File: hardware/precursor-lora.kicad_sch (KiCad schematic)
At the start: 3 parts, among them U2 AP2112K-3.3

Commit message: Fix schematic: add all components and connections
Previous schematic was incomplete skeleton. Now includes:
- U1: RAK3172 module with all 32 pins
- U2: AP2112K-3.3 LDO regulator
- C1, C2: 10uF input/output capacitors
- C3, C4: 100nF decoupling capacitors
- R1: 10K reset pullup
- R2: 10K BOOT0 pulldown
- R3: 1K LED current limit
- LED1: Power indicator
- J1: 8-pin Precursor connector
- J2: U.FL RF connector
- All power symbols and wire connections
- Annotation text for clarity

Embedded lib_symbols so file opens standalone in KiCad 8.
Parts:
- added C3, C4: 100nF, Capacitor_SMD:C_0402_1005Metric, symbol Device:C
- added J1: PRECURSOR_CONN, Connector_PinHeader_1.27mm:PinHeader_2x04_P1.27mm_Vertical, symbol Connector:Conn_01x08_Pin
- added J2: U.FL, Connector_Coaxial:U.FL_Hirose_U.FL-R-SMT-1_Vertical, symbol Connector:Conn_Coaxial
- added LED1: GREEN, LED_SMD:LED_0603_1608Metric, symbol Device:LED
- added R1, R2: 10K, Resistor_SMD:R_0402_1005Metric, symbol Device:R
- added R3: 1K, Resistor_SMD:R_0402_1005Metric, symbol Device:R
- added U1: RAK3172, PrecursorLoRa:RAK3172, symbol PrecursorLoRa:RAK3172
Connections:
- net GND: now also C1.2, C2.2, U2.2 (GND), C3.2, C4.2, J2.2 (Ext), LED1.1 (K), R2.2, U1.23 (GND), U1.28 (GND)
- net VIN_3V7: now also C1.1, U2.1 (VIN), U2.3 (EN)
- new net: J2.1 (In), U1.12 (RF)
- new net: R2.1, U1.22 (BOOT0)
- new net: J1.6 (Pin_6), U1.3 (PA15)
- new net: J1.7 (Pin_7), U1.4 (PB6/UART1_TX)
- new net: R1.2, U1.6 (PA1)
- new net: LED1.2 (A), R3.2
- new net +3V3: C2.1, C3.1, C4.1, R1.1, R3.1, U1.24 (VDD), U2.5 (VOUT)
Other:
- note added: "BOOT0 PULLDOWN (Normal operation)"
- note added: "DECOUPLING CAPACITORS"
- note added: "POWER LED"
- note added: "POWER SUPPLY 3.7V LiPo -> 3.3V LDO"
- note added: "PRECURSOR LORA EXPANSION MODULE Power: 3.7V LiPo -> AP2112K LDO -> 3.3V Interface: UART1 (PB6/PB7) to Precursor FPGA RF: U.FL connector to external antenna"
- note added: "Pin Assignments: 1: UART_TX (to Precursor RX) 2: UART_RX (from Precursor TX) 3: ~RST (active low reset) 4: BUSY (status output) 5: VIN (3.7V) 6: GND 7: NC 8: NC"
- note added: "RESET PULLUP"
- note added: "To Precursor GPIO Header"
- note added: "U.FL RF Connector"
- note removed: "Connector to Precursor 8-pin 1.27mm pitch header"
- note removed: "Power Supply Section Input: 3.7V LiPo Output: 3.3V via AP2112K LDO"
- note removed: "RAK3172 LoRa Module UART1: PB6(TX), PB7(RX) - Primary interface UART2: PA2(TX), PA3(RX) - AT commands"

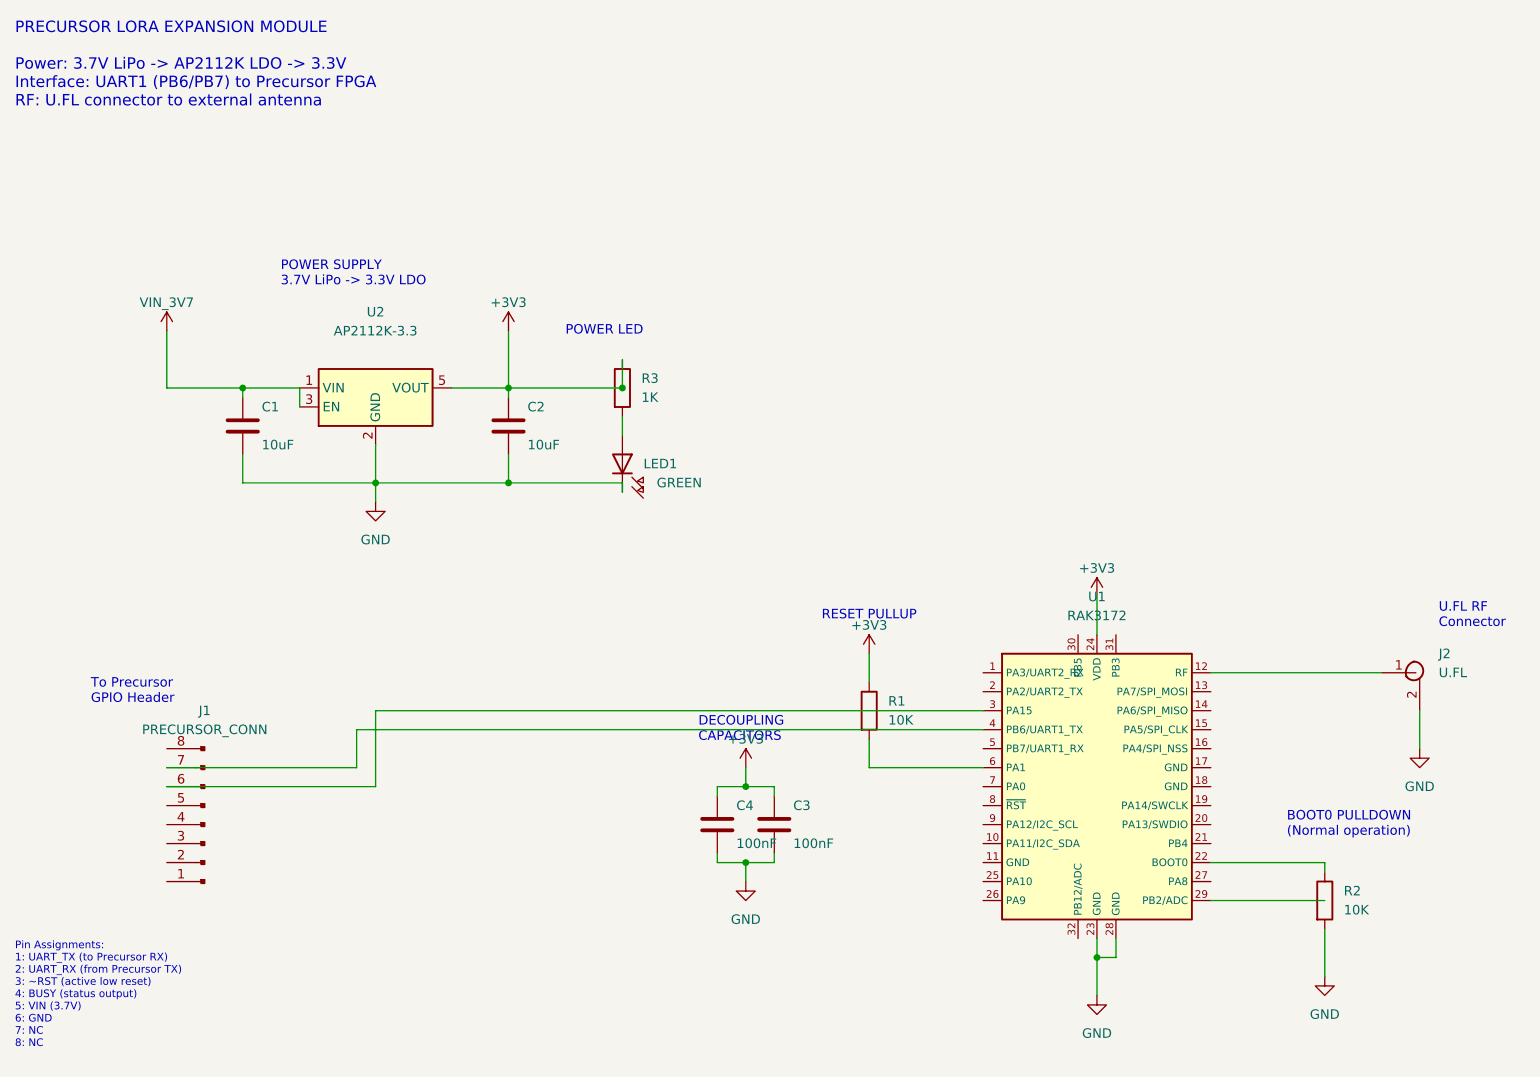
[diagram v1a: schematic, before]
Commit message: Fix schematic wire connections
Corrected wire routing:
- J1.1 now connects to RAK3172 PB6/UART1_TX (pin 4)
- J1.2 now connects to RAK3172 PB7/UART1_RX (pin 5)
- RF wire now correctly routes from RAK3172 pin 12 to U.FL
- Added J1.4 (BUSY) connection to RAK3172 PB5 (pin 30)
- Added J1.5 (VIN) connection to power rail
- Added J1.6 (GND) with GND symbol
- LDO EN pin connected to VIN for always-on operation
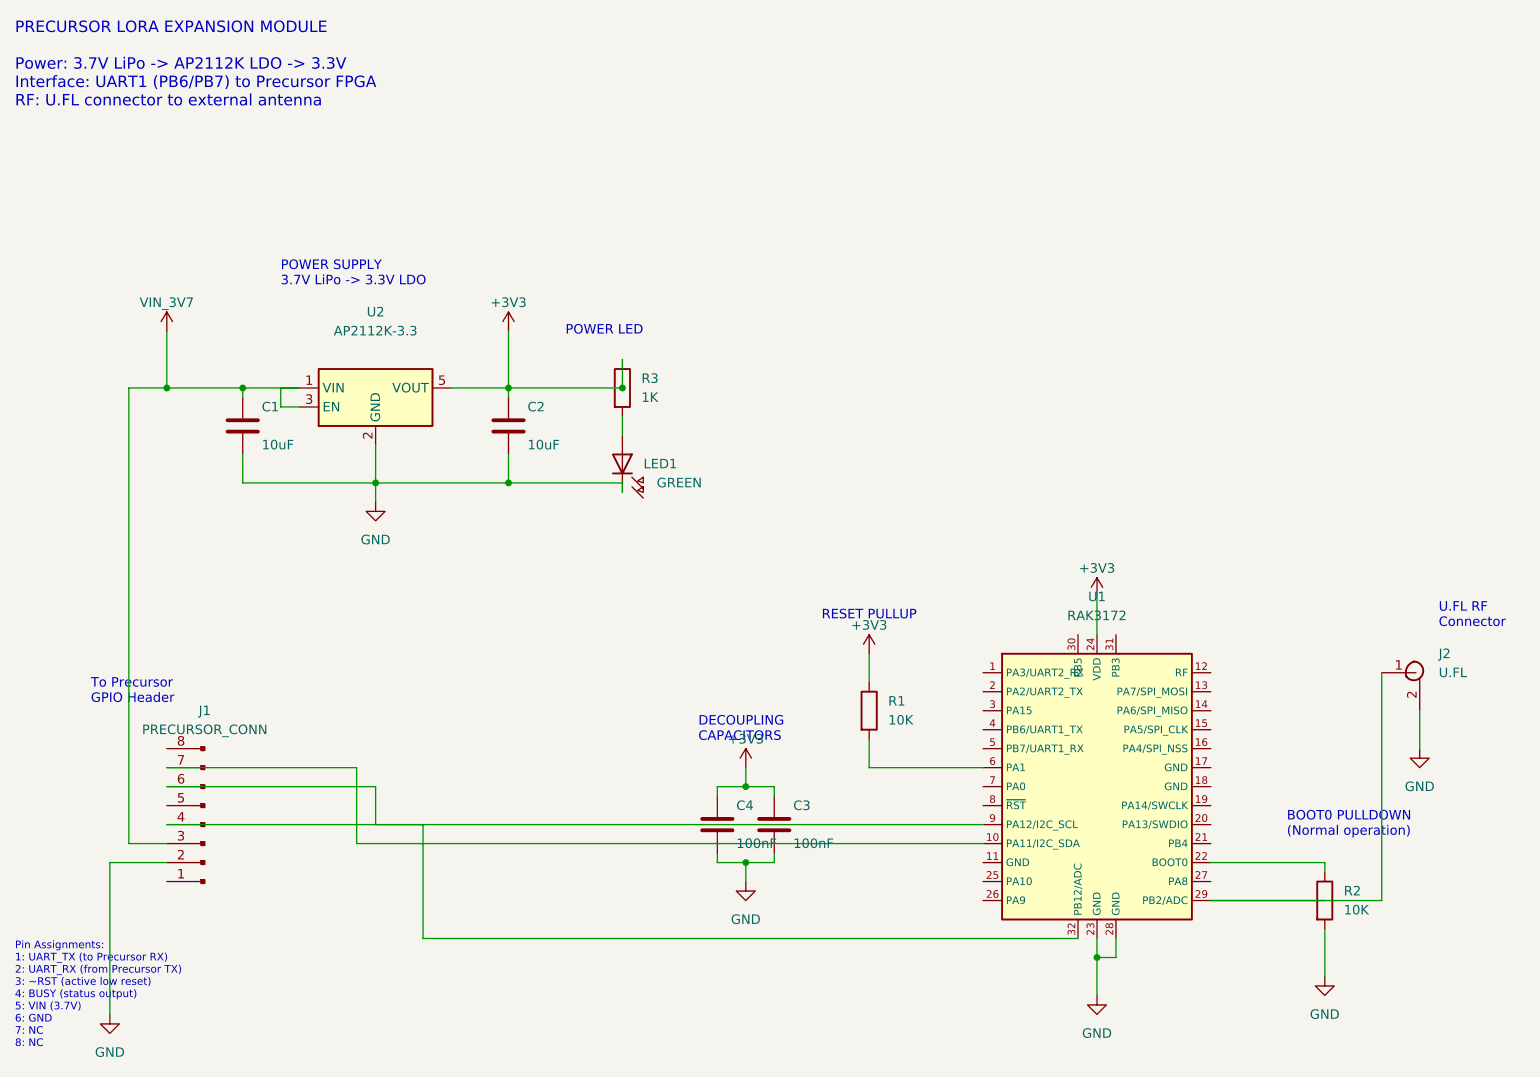
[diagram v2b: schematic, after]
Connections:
- net GND: now also J1.2 (Pin_2)
- net VIN_3V7: now also J1.3 (Pin_3)
- net at U1.10 (PA11/I2C_SDA): now also J1.7 (Pin_7)
- net at U1.12 (RF): no longer J2.1 (In)
- net at U1.29 (PB2/ADC): now also J2.1 (In)
- net at U1.3 (PA15): no longer J1.6 (Pin_6)
- net at U1.32 (PB12/ADC): now also J1.4 (Pin_4), J1.6 (Pin_6), U1.9 (PA12/I2C_SCL)
- net at U1.4 (PB6/UART1_TX): no longer J1.7 (Pin_7)
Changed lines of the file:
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@@
   (wire
     (pts
-      (xy 63.5 71.12) (xy 63.5 68.58)
+      (xy 63.5 71.12) (xy 60.96 71.12)
     )
     (stroke
@@
   (wire
     (pts
+      (xy 60.96 71.12) (xy 60.96 68.58)
+    )
+    (stroke
+      (width 0)
+      (type default)
+    )
+    (uuid "w014b")
+  )
+  (wire
+    (pts
+      (xy 60.96 68.58) (xy 63.5 68.58)
+    )
+    (stroke
+      (width 0)
+      (type default)
+    )
+    (uuid "w014c")
+  )
+  (wire
+    (pts
       (xy 91.44 68.58) (xy 106.68 68.58)
     )
@@
   (wire
     (pts
-      (xy 185.42 106.68) (xy 208.28 106.68)
+      (xy 185.42 137.16) (xy 208.28 137.16)
     )
     (stroke
@@
   (wire
     (pts
+      (xy 208.28 137.16) (xy 208.28 106.68)
+    )
+    (stroke
+      (width 0)
+      (type default)
+    )
+    (uuid "w032b")
+  )
+  (wire
+    (pts
       (xy 213.36 111.76) (xy 213.36 116.84)
     )
@@
   (wire
     (pts
-      (xy 71.12 119.38) (xy 71.12 114.3)
+      (xy 71.12 119.38) (xy 71.12 129.54)
     )
     (stroke
@@
   (wire
     (pts
-      (xy 71.12 114.3) (xy 154.94 114.3)
+      (xy 71.12 129.54) (xy 154.94 129.54)
     )
     (stroke
@@
   (wire
     (pts
-      (xy 73.66 121.92) (xy 73.66 111.76)
+      (xy 73.66 121.92) (xy 73.66 127)
     )
     (stroke
@@
   (wire
     (pts
-      (xy 73.66 111.76) (xy 154.94 111.76)
+      (xy 73.66 127) (xy 154.94 127)
     )
     (stroke
@@
     (uuid "w049")
   )
+  (wire
+    (pts
+      (xy 45.72 127) (xy 80 127)
+    )
+    (stroke
+      (width 0)
+      (type default)
+    )
+    (uuid "w050")
+  )
+  (wire
+    (pts
+      (xy 80 127) (xy 80 142.24)
+    )
+    (stroke
+      (width 0)
+      (type default)
+    )
+    (uuid "w051")
+  )
+  (wire
+    (pts
+      (xy 80 142.24) (xy 167.64 142.24)
+    )
+    (stroke
+      (width 0)
+      (type default)
+    )
+    (uuid "w052")
+  )
+  (wire
+    (pts
+      (xy 45.72 129.54) (xy 40.64 129.54)
+    )
+    (stroke
+      (width 0)
+      (type default)
+    )
+    (uuid "w053")
+  )
+  (wire
+    (pts
+      (xy 40.64 129.54) (xy 40.64 68.58)
+    )
+    (stroke
+      (width 0)
+      (type default)
+    )
+    (uuid "w054")
+  )
+  (wire
+    (pts
+      (xy 40.64 68.58) (xy 45.72 68.58)
+    )
+    (stroke
+      (width 0)
+      (type default)
+    )
+    (uuid "w055")
+  )
+  (wire
+    (pts
+      (xy 45.72 132.08) (xy 38.1 132.08)
+    )
+    (stroke
+      (width 0)
+      (type default)
+    )
+    (uuid "w056")
+  )
+  (wire
+    (pts
+      (xy 38.1 132.08) (xy 38.1 152.4)
+    )
+    (stroke
+      (width 0)
+      (type default)
+    )
+    (uuid "w057")
+  )
   (junction
     (at 55.88 68.58)
@@
     (uuid "t008")
   )
+  (symbol
+    (lib_id "power:GND")
+    (at 38.1 152.4 0)
+    (unit 1)
+    (exclude_from_sim no)
+    (in_bom yes)
+    (on_board yes)
+    (dnp no)
+    (property "Reference" "#PWR11"
+      (at 38.1 158.75 0)
+      (effects
+        (font
+          (size 1.27 1.27)
+        )
+        (hide yes)
+      )
+    )
+    (property "Value" "GND"
+      (at 38.1 157.48 0)
+      (effects
+        (font
+          (size 1.27 1.27)
+        )
+      )
+    )
+    (property "Footprint" ""
+      (at 38.1 152.4 0)
+      (effects
+        (font
+          (size 1.27 1.27)
+        )
+        (hide yes)
+      )
+    )
+    (property "Datasheet" ""
+      (at 38.1 152.4 0)
+      (effects
+        (font
+          (size 1.27 1.27)
+        )
+        (hide yes)
+      )
+    )
+    (pin "1"
+      (uuid "pin-pwr11-1")
+    )
+  )
+  (junction
+    (at 45.72 68.58)
+    (diameter 0)
+    (color 0 0 0 0)
+    (uuid "j009")
+  )
   (sheet_instances
